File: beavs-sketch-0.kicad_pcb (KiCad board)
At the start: 4 copper layers, 50 x 70 mm, 126 parts, among them J1 USB_C_Receptacle_USB2.0_16P, J10 Conn_01x03, J11 Conn_01x03, J12 Micro_SD_Card, J2 Conn_Coaxial, J3 Conn_01x02, J4 Conn_Coaxial, J5 Conn_01x02, J6 Conn_01x03, J7 Conn_01x03, J8 Conn_01x03, J9 Conn_01x03, Q1 SiS402DN, Q2 SiS402DN, SW1 SW_Push, SW2 SW_Push, U1 RP2040, U10 INA745A, U11 INA745A, U12 INA745A, U13 INA745A, U14 ISM6HG256X, U15 SN74LVC8T245, U16 SRV05-4, U17 SRV05-4, U18 LIS2MDL, U19 LM74502, U2 W25Q128JVS, U3 MS5607-02BA, U4 RFM95W-915S2, U5 MAX-M10S, U6 INA745A, U7 AMS1117-3.3, U8 AMS1117-5.0, U9 INA745A, Y1 Crystal_GND24

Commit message: I may be stupid
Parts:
- removed C46: 220n, Capacitor_SMD:C_0402_1005Metric
- removed the REF** at (213.7, 56.7)
- added Q3: AO3401A, Package_TO_SOT_SMD:SOT-23, F.Cu at (207.2, 55.0)
- added R14: R_Small, Resistor_SMD:R_0402_1005Metric, F.Cu at (202.0, 58.2)
- C45: value 220n -> C_Small
- R2: value 100 -> R; footprint Resistor_SMD:R_0402_1005Metric -> Resistor_SMD:R_0805_2012Metric
- U19: value LM74502 -> LM74700; footprint Package_TO_SOT_SMD:SOT-23-8 -> Package_TO_SOT_SMD:SOT-23-6
- moved R2 14.1 mm to (194.0, 59.8)
- moved U19 1.59 mm to (203.2, 56.1), turned to 0 degrees
- moved JP1 1.57 mm to (219.2, 59.0)
- moved J3 1.50 mm to (189.2, 55.6)
- moved Q1 1.43 mm to (199.2, 57.0)
- moved J4 1.40 mm to (210.3, 57.7)
- moved C45 1.40 mm to (203.4, 53.9), turned to 180 degrees
- moved C19 0.90 mm to (193.8, 65.8)
- moved U6 0.61 mm to (193.2, 62.8)
- moved Q2 0.18 mm to (197.9, 61.8)
- moved C8 0.13 mm to (204.9, 91.5)
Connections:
- C45 pad 1: Net-(U19-EN/UVLO) -> Net-(U19-ANODE)
- Q1 pad 1: Net-(U19-SRC) -> Net-(U19-ANODE)
- Q1 pad 2: Net-(U19-SRC) -> Net-(U19-ANODE)
- Q1 pad 3: Net-(U19-SRC) -> Net-(U19-ANODE)
- Q2 pad 1: Net-(U19-SRC) -> Net-(U19-ANODE)
- Q2 pad 2: Net-(U19-SRC) -> Net-(U19-ANODE)
- Q2 pad 3: Net-(U19-SRC) -> Net-(U19-ANODE)
- Q2 pad 4: Net-(Q1-G) -> Net-(Q2-G)
- R2 pad 1: Net-(Q1-G) -> Net-(J3-Pin_2)
- R2 pad 2: Net-(C46-Pad1) -> Net-(U19-ANODE)
- U1 pad 11: unconnected-(U1-GPIO8-Pad11) -> /mcu/SERVO_POWER_EN
- U19 pad 1: Net-(U19-EN/UVLO) -> Net-(U19-VCAP)
- U19 pad 4: Net-(U19-VCAP) -> +BATT
- U19 pad 5: Net-(U19-EN/UVLO) -> Net-(Q2-G)
- U19 pad 6: Net-(Q1-G) -> Net-(U19-ANODE)
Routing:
- net /mcu/SERVO_POWER_EN: track 0.00 -> 47.6 mm, vias 0 -> 2
- net Net-(U19-ANODE): track 0.00 -> 17.6 mm, vias 0 -> 3
- net Net-(Q2-G): track 0.00 -> 15.7 mm, vias 0 -> 2
- net +BATT: track 10.0 -> 18.8 mm, vias 53 -> 55
- net Net-(U19-EN/UVLO): track 6.23 -> 0.00 mm, vias 2 -> 0
- net Net-(Q1-G): track 17.8 -> 11.6 mm, vias 4 -> 2
- net Net-(J3-Pin_2): track 0.00 -> 5.04 mm, vias 14 -> 11
- net Net-(U19-SRC): track 4.23 -> 0.00 mm
- net /servos/S4: track 65.3 -> 66.6 mm
- net /servos/S2: track 60.3 -> 61.3 mm
- net Net-(C46-Pad1): track 0.92 -> 0.00 mm
- net Net-(J4-In): track 4.25 -> 5.11 mm
- net Net-(JP1-B): track 14.9 -> 14.0 mm
- net /Sensors/SDA: track 108.6 -> 109.3 mm
- net GND: track 29.5 -> 28.8 mm, vias 236 -> 234
- added copper zone on F.Cu, net Net-(U19-ANODE)
- removed copper zone on F.Cu, net Net-(U19-SRC)

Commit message: definitely stupid
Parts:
- removed Q1: SiS402DN, Package_SO:Vishay_PowerPAK_1212-8_Single
- removed Q3: AO3401A, Package_TO_SOT_SMD:SOT-23
- removed R14: R_Small, Resistor_SMD:R_0402_1005Metric
- added C46: 220n, Capacitor_SMD:C_0402_1005Metric, F.Cu at (202.0, 57.0)
- added D11: D_Schottky, Diode_SMD:D_SOD-123, F.Cu at (201.2, 61.4)
- added REF**: MountingHole_2.2mm_M2, MountingHole:MountingHole_2.2mm_M2, F.Cu at (215.1, 57.4)
- C45: value C_Small -> 220n
- R2: value R -> 300; footprint Resistor_SMD:R_0805_2012Metric -> Resistor_SMD:R_1206_3216Metric
- moved R2 7.16 mm to (200.4, 56.6), turned to -90 degrees
- moved C45 3.71 mm to (204.4, 57.5), turned to 0 degrees
- moved U19 1.56 mm to (204.5, 55.2), turned to 180 degrees
- moved C19 0.61 mm to (193.7, 65.2)
- moved U6 0.60 mm to (193.2, 62.2)
- moved Q2 0.32 mm to (198.2, 62.0)
- moved J3 0.13 mm to (189.2, 55.7)
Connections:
- C45 pad 1: Net-(U19-ANODE) -> Net-(J3-Pin_2)
- Q2 pad 1: Net-(U19-ANODE) -> Net-(J3-Pin_2)
- Q2 pad 2: Net-(U19-ANODE) -> Net-(J3-Pin_2)
- Q2 pad 3: Net-(U19-ANODE) -> Net-(J3-Pin_2)
- R2 pad 2: Net-(U19-ANODE) -> Net-(D11-A)
- U19 pad 3: unconnected-(U19-EN-Pad3) -> /mcu/SERVO_POWER_EN
- U19 pad 6: Net-(U19-ANODE) -> Net-(J3-Pin_2)
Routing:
- net Net-(U19-ANODE): track 17.6 -> 0.00 mm, vias 3 -> 0
- net Net-(Q1-G): track 11.6 -> 0.00 mm, vias 2 -> 0
- net Net-(J3-Pin_2): track 5.04 -> 1.47 mm, vias 11 -> 0
- net Net-(Q2-G): track 15.7 -> 12.4 mm
- net +BATT: track 18.8 -> 21.9 mm
- net Net-(D11-A): track 0.00 -> 2.02 mm
- net /mcu/SERVO_POWER_EN: track 47.6 -> 48.6 mm
- net GND: track 28.8 -> 28.6 mm, vias 234 -> 233
- removed copper zone on F.Cu, net Net-(U19-ANODE)

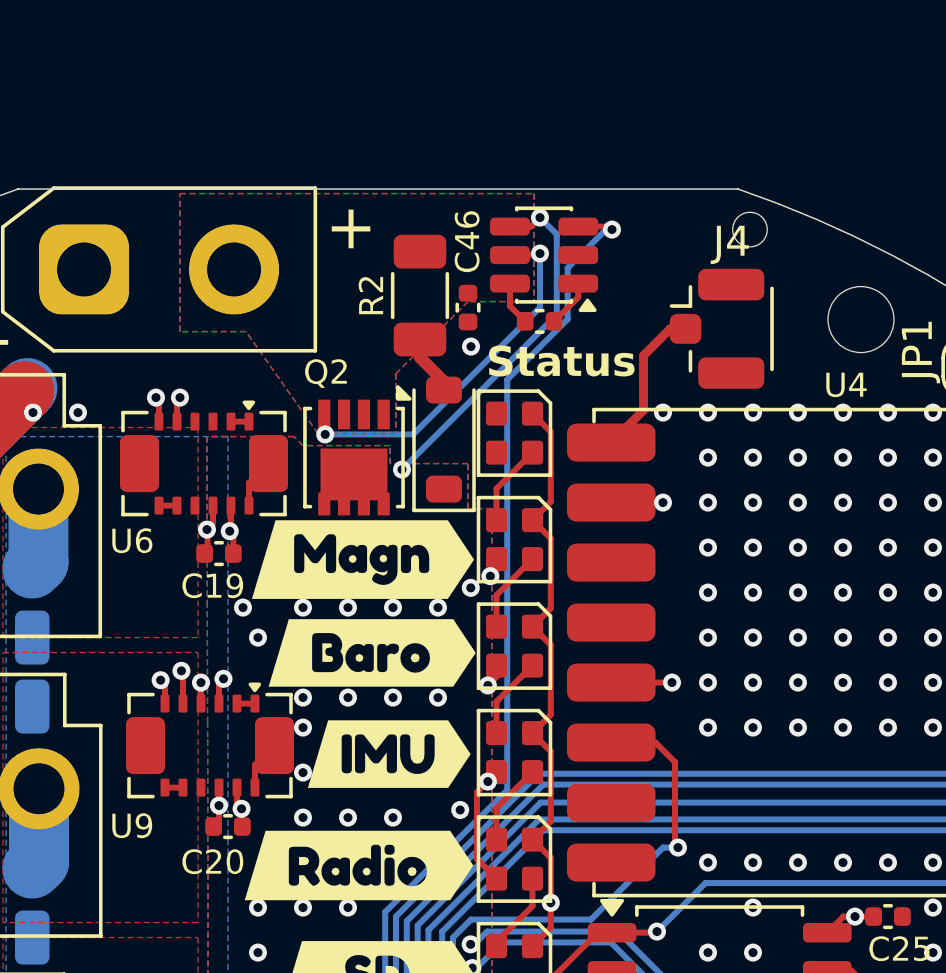
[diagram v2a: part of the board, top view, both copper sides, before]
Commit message: swapped to a reverse polarity + inrush scheme that might actually work
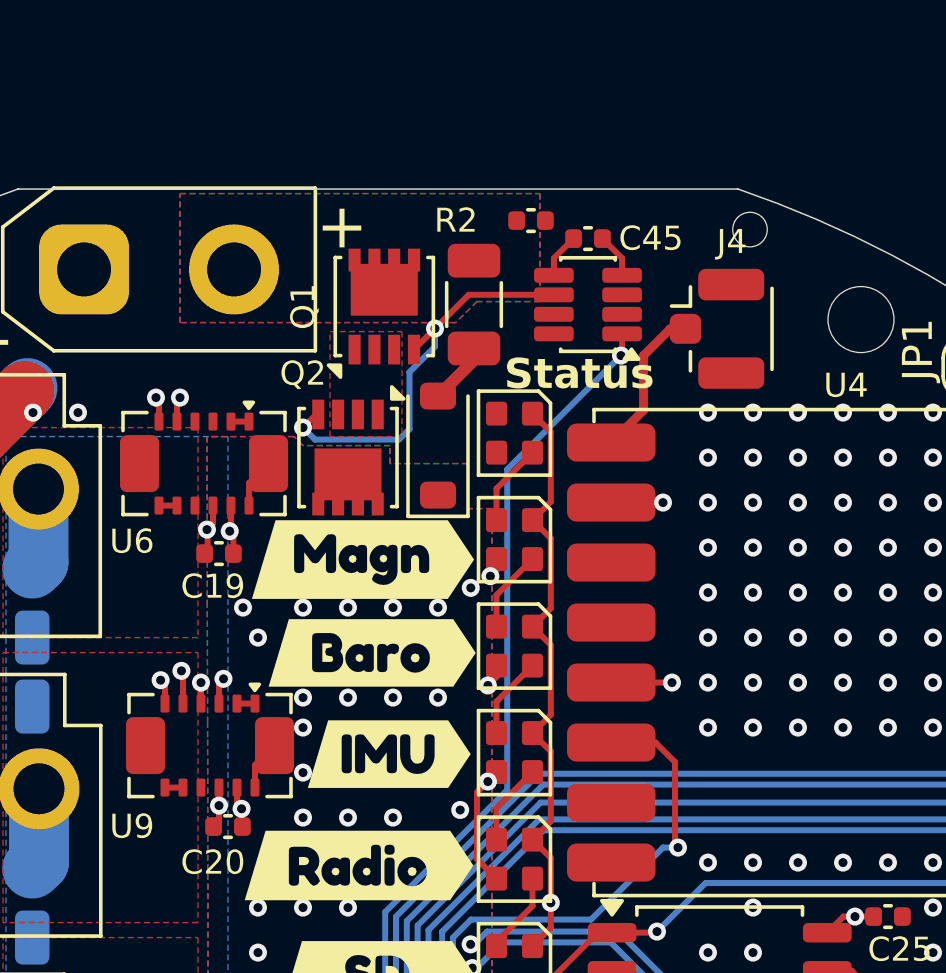
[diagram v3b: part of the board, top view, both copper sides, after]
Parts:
- added Q1: SiS402DN, Package_SO:Vishay_PowerPAK_1212-8_Single, F.Cu at (199.2, 57.0)
- U19: value LM74700 -> LM74502; footprint Package_TO_SOT_SMD:SOT-23-6 -> Package_TO_SOT_SMD:SOT-23-8
- moved C46 3.58 mm to (204.1, 54.1), turned to 0 degrees
- moved C45 3.20 mm to (206.0, 54.7)
- moved U19 2.20 mm to (206.0, 56.9)
- moved R2 1.82 mm to (202.2, 56.9)
- moved D11 0.28 mm to (201.0, 61.6)
- moved Q2 0.20 mm to (198.0, 62.0)
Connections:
- Q2 pad 1: Net-(J3-Pin_2) -> Net-(U19-SRC)
- Q2 pad 2: Net-(J3-Pin_2) -> Net-(U19-SRC)
- Q2 pad 3: Net-(J3-Pin_2) -> Net-(U19-SRC)
- Q2 pad 4: Net-(Q2-G) -> Net-(Q1-G)
- U19 pad 1: Net-(U19-VCAP) -> /mcu/SERVO_POWER_EN
- U19 pad 3: /mcu/SERVO_POWER_EN -> unconnected-(U19-NC-Pad3)
- U19 pad 4: +BATT -> Net-(U19-VCAP)
- U19 pad 5: Net-(Q2-G) -> Net-(J3-Pin_2)
- U19 pad 6: Net-(J3-Pin_2) -> Net-(Q1-G)
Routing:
- net Net-(Q1-G): track 0.00 -> 13.7 mm, vias 0 -> 2
- net Net-(Q2-G): track 12.4 -> 0.00 mm, vias 2 -> 0
- net +BATT: track 21.9 -> 10.0 mm, vias 55 -> 53
- net /mcu/SERVO_POWER_EN: track 48.6 -> 44.0 mm
- net GND: vias 233 -> 231
- added copper zone on F.Cu, net Net-(U19-SRC)

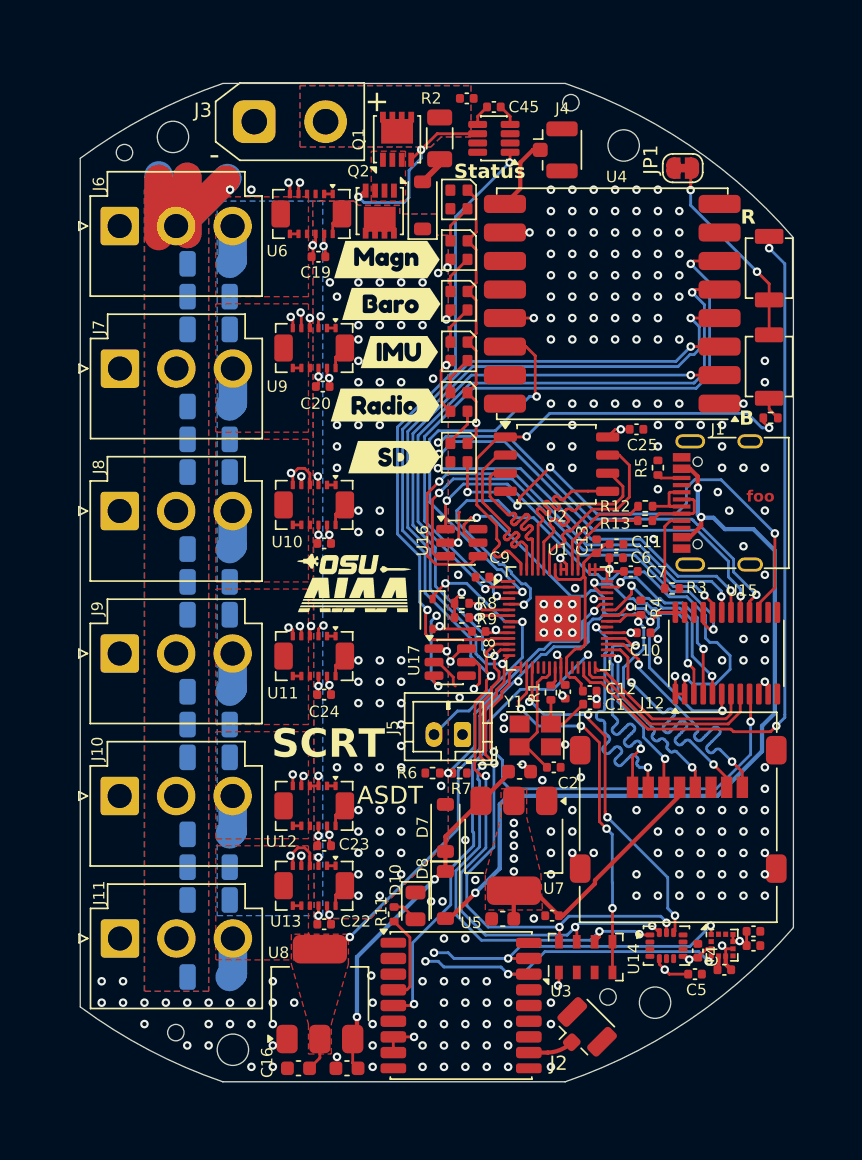
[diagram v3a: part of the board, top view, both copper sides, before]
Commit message: finished power, checked most sensor schematics
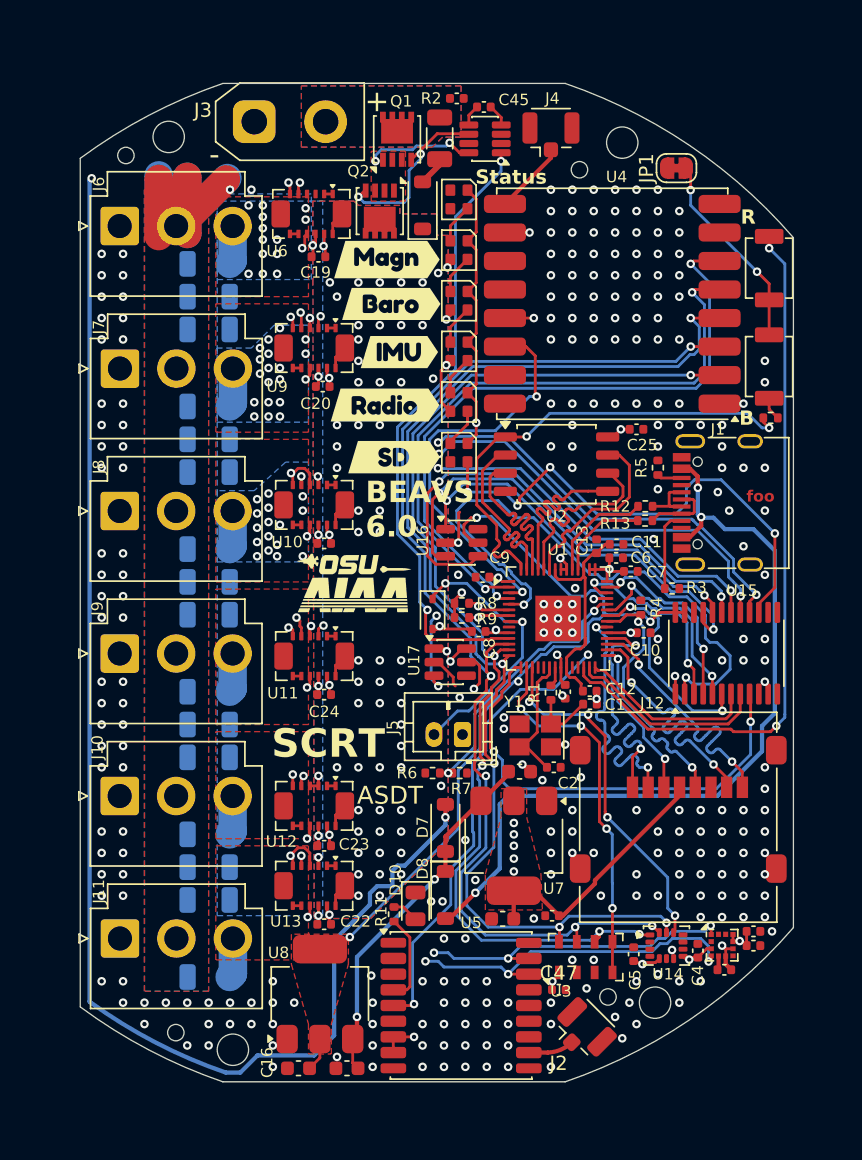
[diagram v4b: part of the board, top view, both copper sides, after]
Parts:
- added C47: 100n, Capacitor_SMD:C_0402_1005Metric, F.Cu at (210.6, 116.6)
- moved REF** 4.74 mm to (212.0, 59.1)
- moved C5 4.52 mm to (215.8, 114.1), turned to 90 degrees
- moved J4 1.10 mm to (210.0, 56.6), turned to 90 degrees
- moved C45 0.70 mm to (205.3, 54.7)
- moved C46 0.70 mm to (203.4, 54.1)
- moved U19 0.62 mm to (205.4, 56.9)
- moved JP1 0.44 mm to (218.8, 59.0)
- moved REF** 0.30 mm to (183.2, 56.8)
- moved REF** 0.22 mm to (180.2, 58.1)
- moved REF** 0.22 mm to (215.0, 57.2)
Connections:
- net /mcu/SERVO_POWER_EN renamed /Power/EN
- C45 pad 1: Net-(J3-Pin_2) -> Net-(D7-A)
- C46 pad 1: Net-(J3-Pin_2) -> Net-(D7-A)
- D7 pad 2: +BATT -> Net-(D7-A)
- J3 pad 2: Net-(J3-Pin_2) -> Net-(D7-A)
- Q1 pad 5: Net-(J3-Pin_2) -> Net-(D7-A)
- R2 pad 1: Net-(J3-Pin_2) -> Net-(D7-A)
- U10 pad 10: unconnected-(U10-ALERT-Pad10) -> GND
- U11 pad 10: unconnected-(U11-ALERT-Pad10) -> GND
- U12 pad 10: unconnected-(U12-ALERT-Pad10) -> GND
- U13 pad 10: unconnected-(U13-ALERT-Pad10) -> GND
- U18 pad 7: unconnected-(U18-DRDY-Pad7) -> GND
- U19 pad 5: Net-(J3-Pin_2) -> Net-(D7-A)
- U6 pad 10: unconnected-(U6-ALERT-Pad10) -> GND
- U9 pad 10: unconnected-(U9-ALERT-Pad10) -> GND
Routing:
- net Net-(D7-A): track 0.00 -> 108.4 mm, vias 0 -> 2
- net Net-(U19-SRC): track 0.00 -> 7.60 mm, vias 0 -> 2
- net GND: track 28.6 -> 34.3 mm, vias 231 -> 298
- net /Sensors/SDA: track 109.0 -> 113.7 mm
- net Net-(J3-Pin_2): track 1.50 -> 0.00 mm
- net /Sensors/SCL: track 112.8 -> 113.8 mm
- net +3V3: track 63.1 -> 62.4 mm
- net /servos/S4: track 66.6 -> 67.4 mm
- net Net-(Q1-G): track 13.7 -> 12.9 mm
- net Net-(J8-Pin_3): vias 0 -> 16
- net Net-(J7-Pin_3): vias 0 -> 18
- net Net-(J6-Pin_3): vias 0 -> 13
- added copper zone on B.Cu, net Net-(D7-A)
- added copper zone on F.Cu, net Net-(D7-A)
- added copper zone on B.Cu, net Net-(J6-Pin_3)
- added copper zone on B.Cu, net Net-(J7-Pin_3)
- added copper zone on B.Cu, net Net-(J8-Pin_3)
- removed copper zone on B.Cu, net Net-(J3-Pin_2)
- removed copper zone on F.Cu, net Net-(J3-Pin_2)
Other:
- board text added: "BEAVS 6.0"
- board text added: "⌀74mm"
- board text removed: "d=74mm"

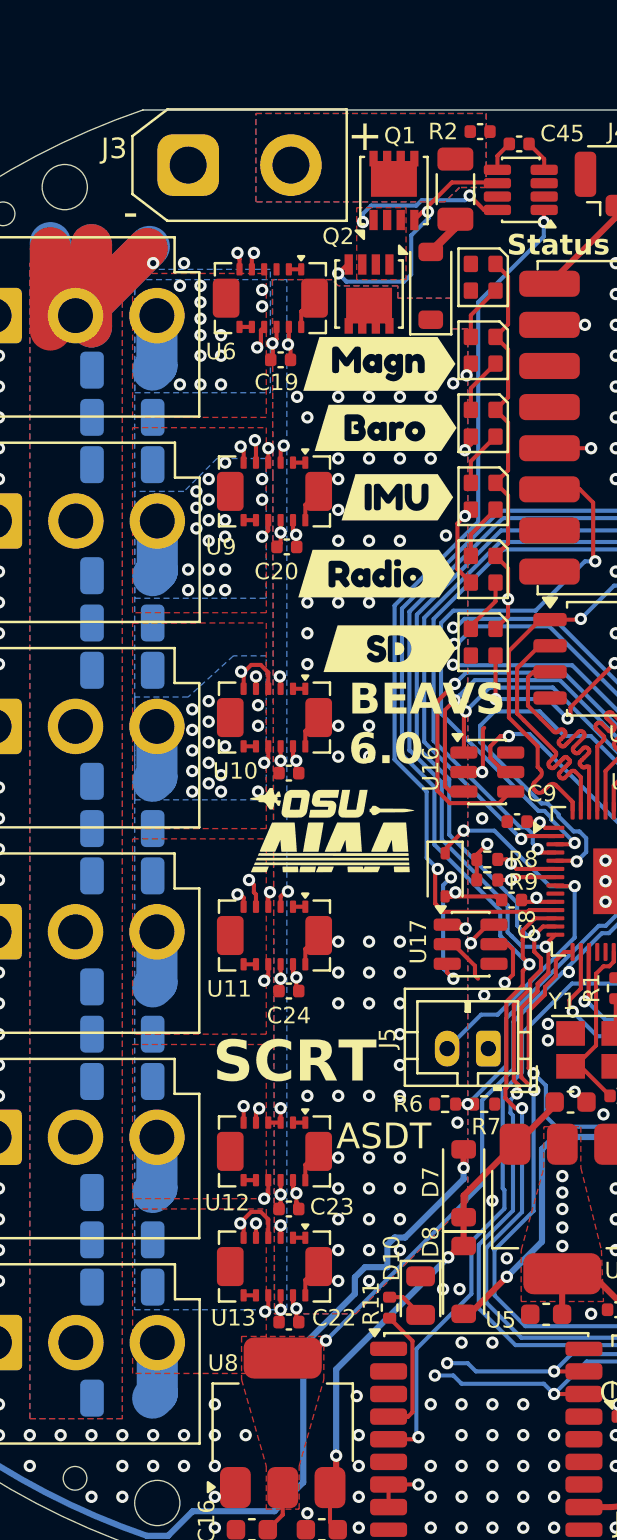
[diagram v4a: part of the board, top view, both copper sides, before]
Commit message: bigger pours for FETs, various cleanup, switching to different level shifter
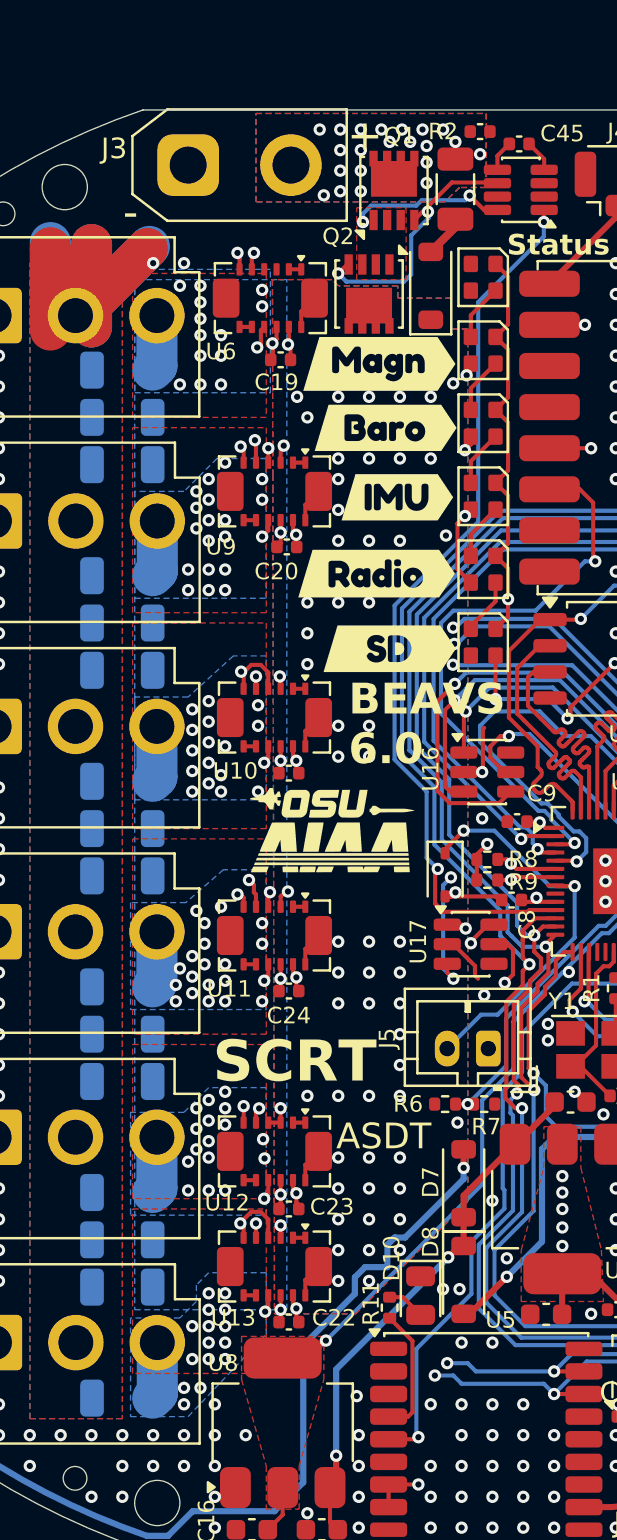
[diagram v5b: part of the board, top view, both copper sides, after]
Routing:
- net Net-(J9-Pin_3): vias 0 -> 19
- net Net-(J11-Pin_3): vias 0 -> 15
- net Net-(J10-Pin_3): vias 0 -> 16
- net Net-(D7-A): vias 2 -> 23
- added copper zone on B.Cu, net Net-(J10-Pin_3)
- added copper zone on B.Cu, net Net-(J11-Pin_3)
- added copper zone on B.Cu, net Net-(J9-Pin_3)
